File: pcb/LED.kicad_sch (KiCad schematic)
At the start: 2 parts

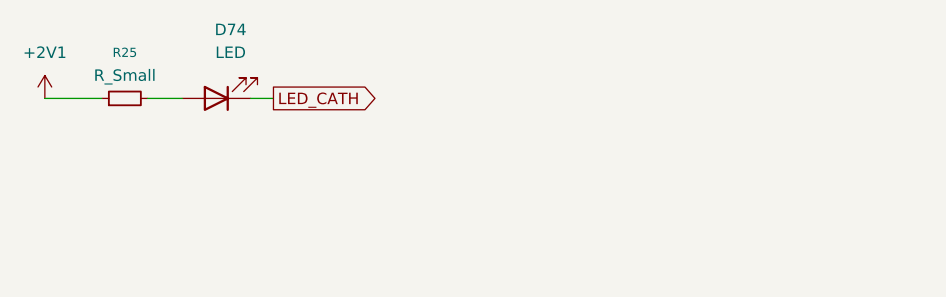
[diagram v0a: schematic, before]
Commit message: A  notes/bypasscaps A  notes/keytravel M  notes/leds A  notes/muxadc M  notes/notes A  notes/pulldown M  notes/scan A  notes/swupdate M  pcb/LED.kicad_sch M  pcb/pcb.kicad_pcb M  pcb/pcb.kicad_prl M  pcb/pcb.kicad_pro M  pcb/pcb.kicad_sch M  pcb/switch.kicad_sch M  placefp.py A  tmr-footprints/C_0402_1005Metric.kicad_mod M  tmr-footprints/C_0603_1608Metric.kicad_mod D  tmr-footprints/C_1206_3216Metric.kicad_mod A  tmr-footprints/Ezurio_BL54L15_Module.kicad_mod A  tmr-footprints/LED_1206_3216Metric_ReverseMount_Hole2.1mm.kicad_mod A  tmr-footprints/Murata_DFE201210U.kicad_mod A  tmr-footprints/R_0402_1005Metric.kicad_mod M  tmr-footprints/SOT-23-3.kicad_mod M  tmr-symbols.kicad_sym
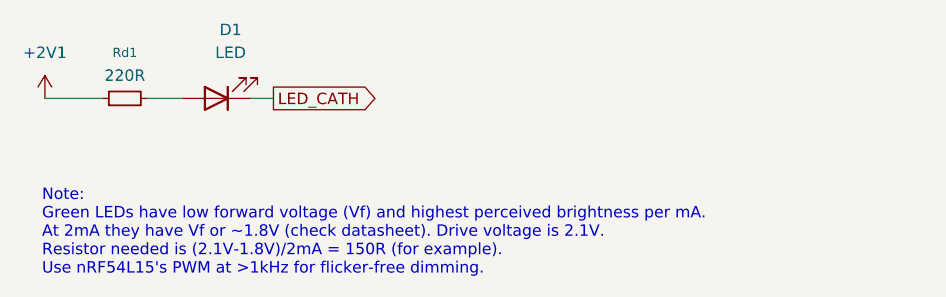
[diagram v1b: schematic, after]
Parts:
- D1: renamed from D74; footprint (none) -> tmr-lib:LED_1206_3216Metric_ReverseMount_Hole2.1mm
- Rd1: renamed from R25; value R_Small -> 220R; footprint (none) -> tmr-lib:R_0402_1005Metric
